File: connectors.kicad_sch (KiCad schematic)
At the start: 1 part, among them J2 SM04B-SRSS-TB

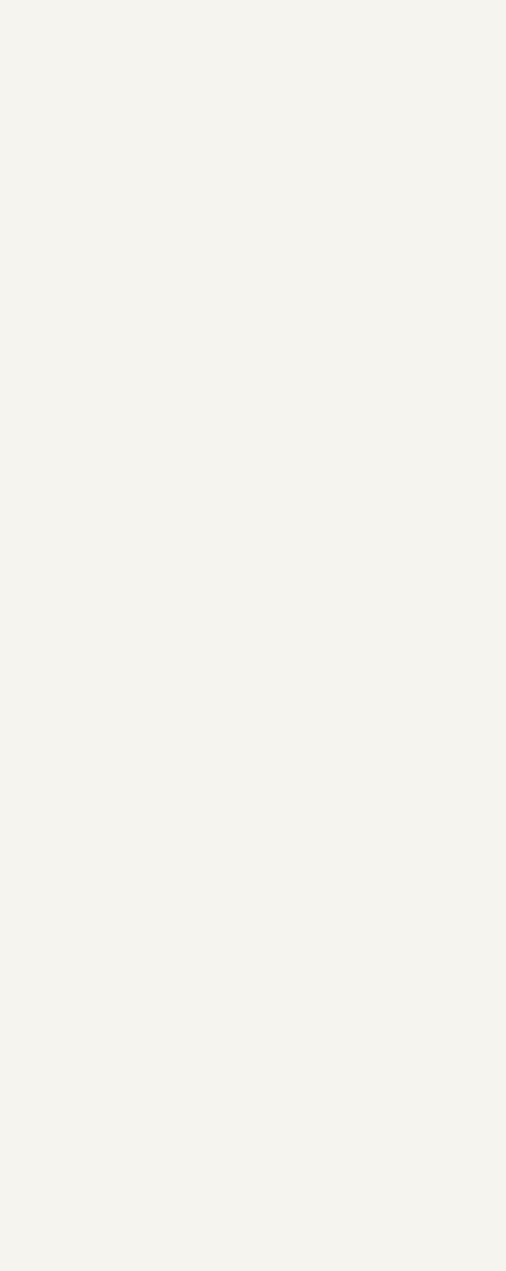
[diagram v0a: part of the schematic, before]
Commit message: finished buck schematic and designed solder pads footprints
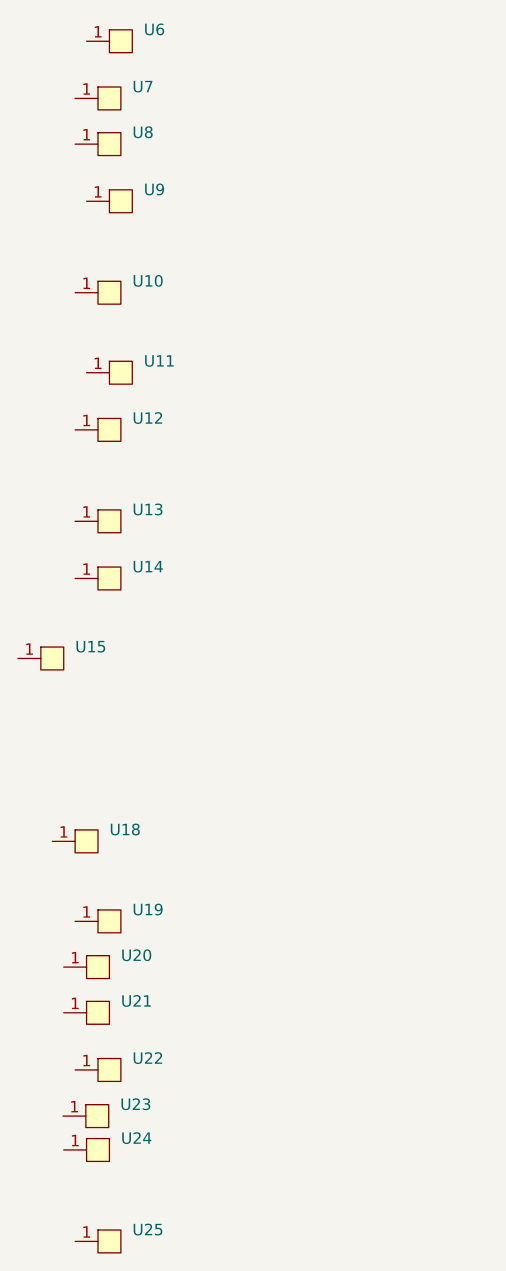
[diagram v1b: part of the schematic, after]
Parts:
- added U10, U11, U12, U13, U14, U15, U18, U19, U20, U21, U22, U23, U24, U25, U6, U7, U8, U9: ~, fcg4_fp:soldering_pad, symbol fcg4:SolderPad

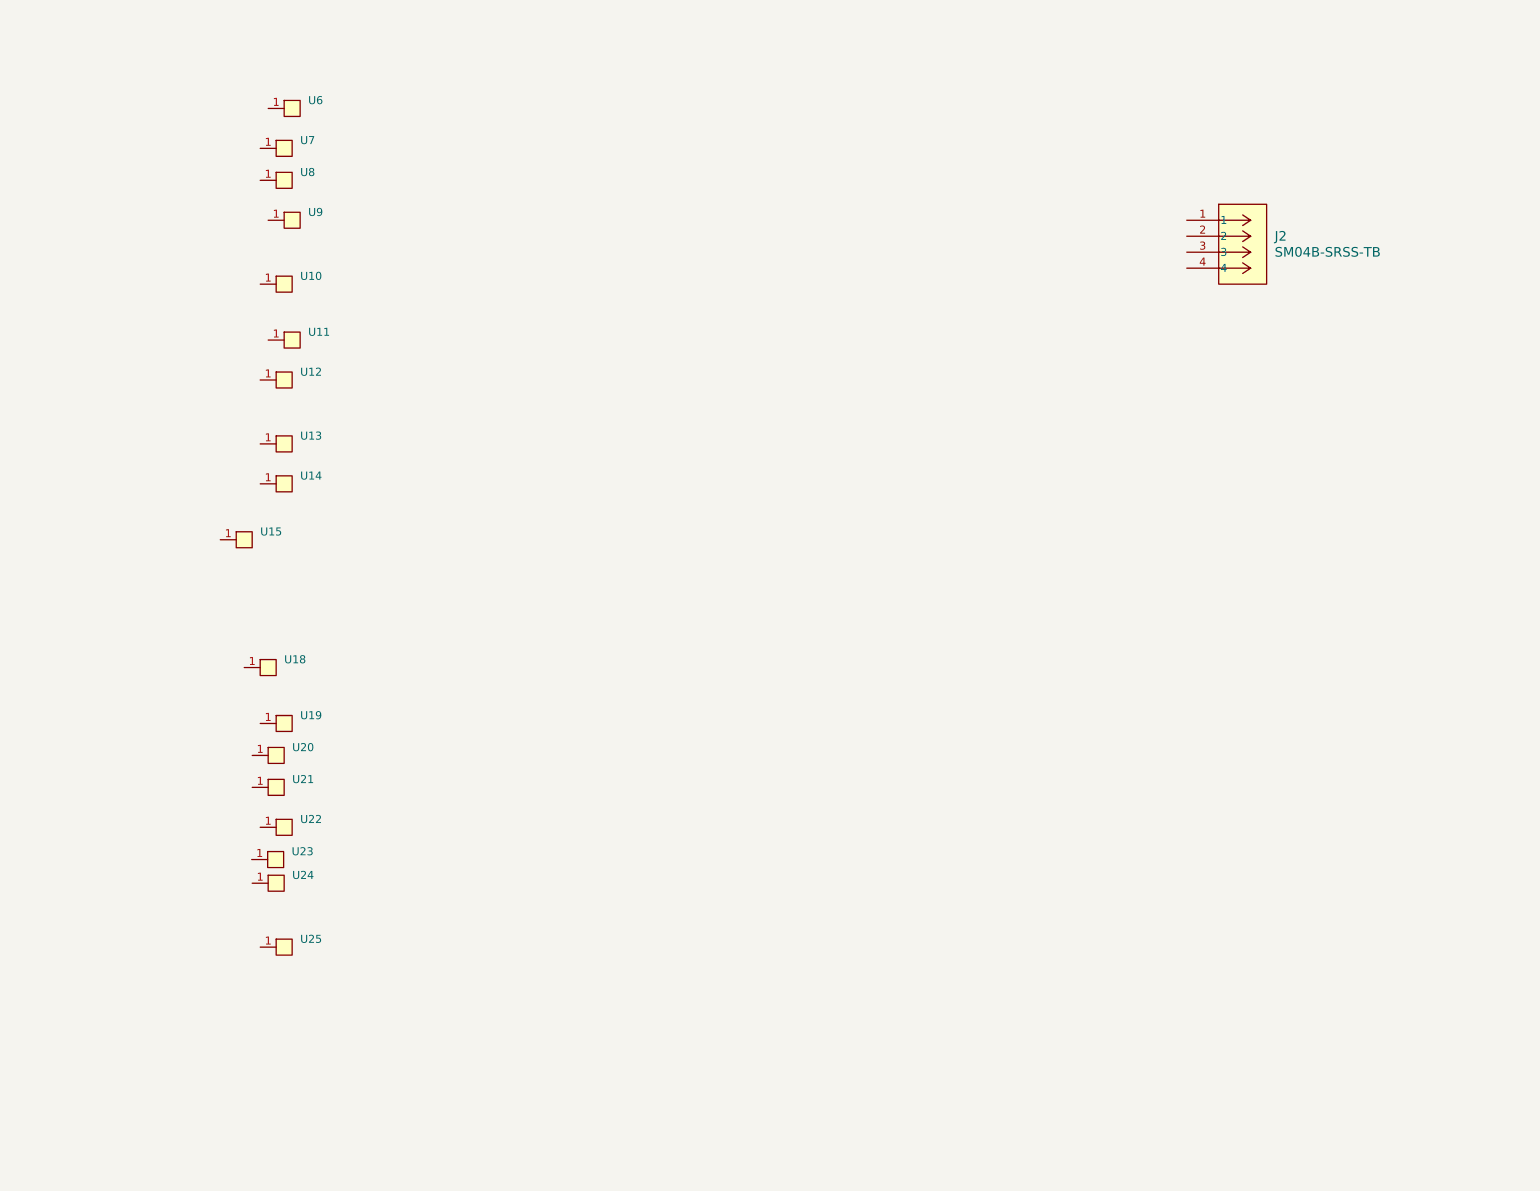
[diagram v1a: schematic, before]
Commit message: add wiring to soldering pads for uart, dji, and esc
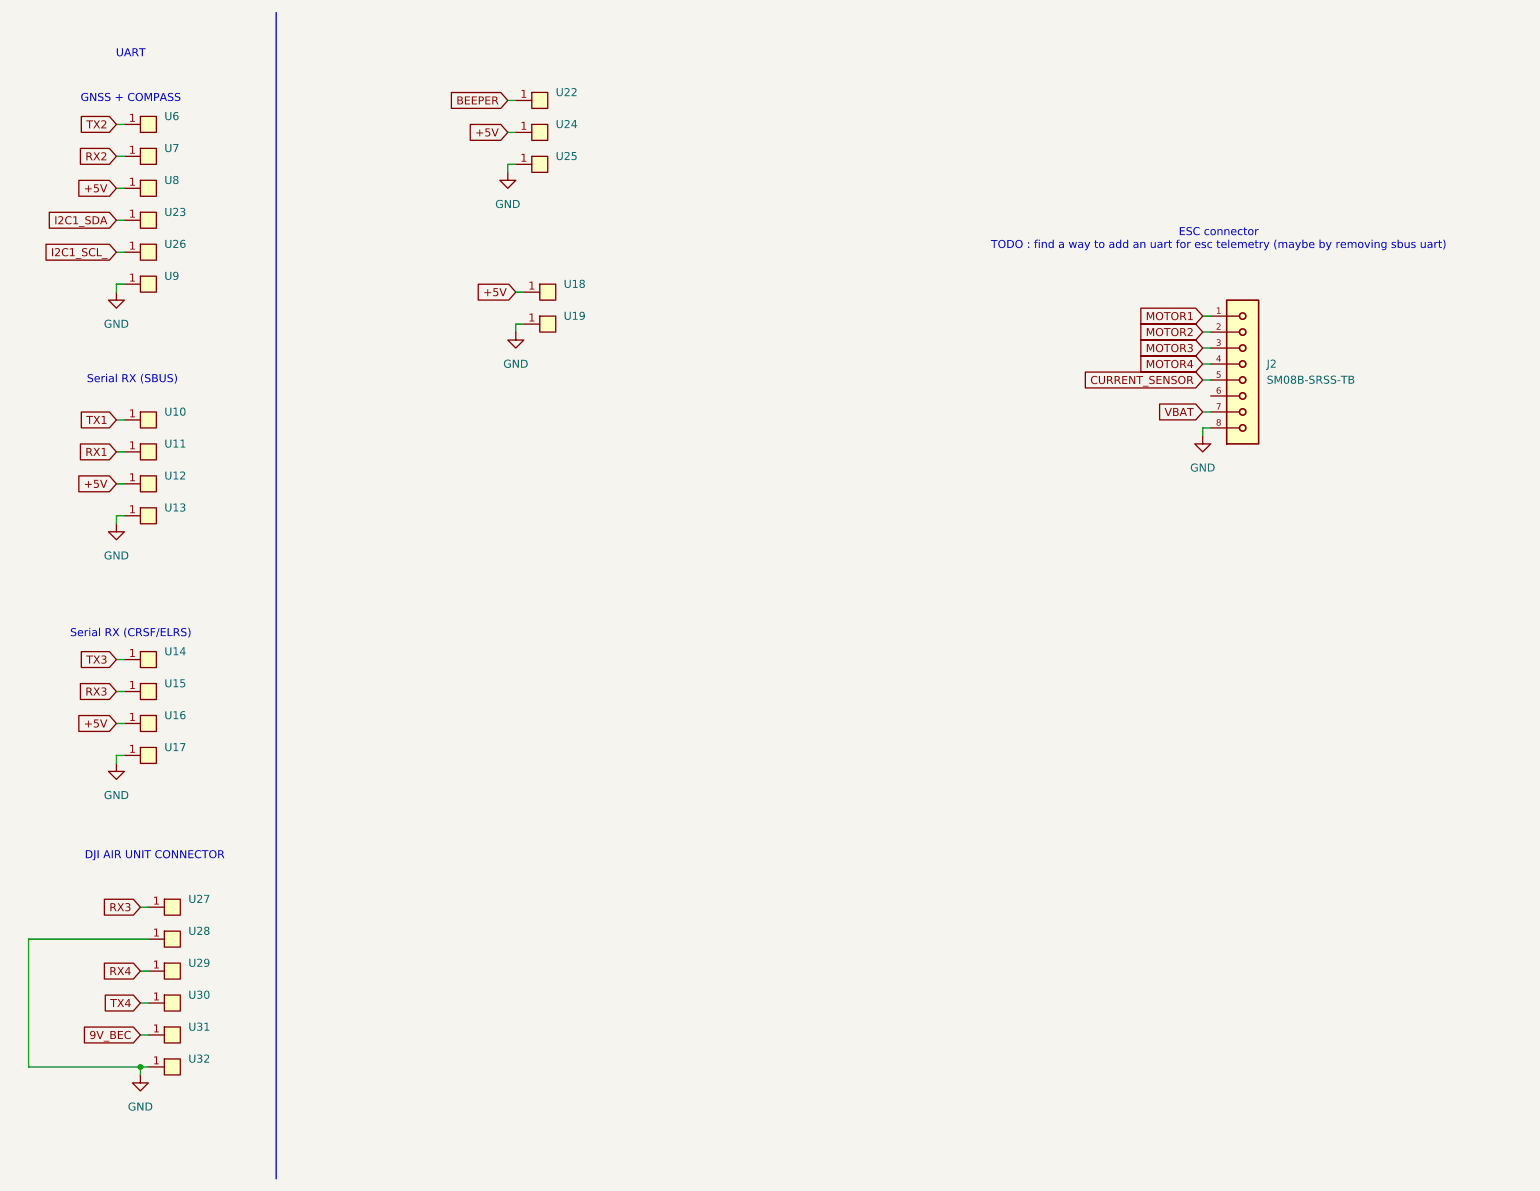
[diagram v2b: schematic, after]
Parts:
- removed J2: SM04B-SRSS-TB, fcg4_fp:CONN_SM04B-SRSS-TB_JST, symbol fcg4:SM04B-SRSS-TB
- removed U20, U21: ~, fcg4_fp:soldering_pad, symbol fcg4:SolderPad
- added J2: SM08B-SRSS-TB, fcg4_fp:JST_SM08B-SRSS-TB, symbol fcg4:SM08B-SRSS-TB
- added U16, U17, U26, U27, U28, U29, U30, U31, U32: ~, fcg4_fp:soldering_pad, symbol fcg4:SolderPad
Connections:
- net RX3: now reaches U15.1
- net RX3: now also U27.1
- net GND: now reaches U13.1
- net GND: now also U19.1, U25.1, U9.1, J2.8, U17.1, U28.1, U32.1
- net BEEPER: now reaches U22.1
- net RX2: now reaches U7.1
- net TX3: now reaches U14.1
- net I2C1_SDA: now reaches U23.1
- net +5V: now reaches U8.1
- net +5V: now also U12.1, U18.1, U24.1, U16.1
- net TX1: now reaches U10.1
- net TX2: now reaches U6.1
- net RX1: now reaches U11.1
- new net 9V_BEC: U31.1
- new net CURRENT_SENSOR: J2.5
- new net I2C1_SCL_: U26.1
- new net MOTOR1: J2.1
- new net MOTOR2: J2.2
- new net MOTOR3: J2.3
- new net MOTOR4: J2.4
- new net RX4: U29.1
- new net TX4: U30.1
- new net VBAT: J2.7
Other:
- note added: "DJI AIR UNIT CONNECTOR"
- note added: "ESC connector TODO : find a way to add an uart for esc telemetry (maybe by removing sbus uart)"
- note added: "GNSS + COMPASS"
- note added: "Serial RX (CRSF/ELRS)"
- note added: "Serial RX (SBUS)"
- note added: "UART"
- moved on the sheet: U6, U7, U8, U9

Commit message: - Removed SBUS receiver support in uart1 and added esc telemetry in uart2 - Added a new Mounting Hole symbol with properties and graphical representation in the schematic (fcg4.kicad_sch). (MountingHoles_30.5x30.5mm_Standard.kicad_mod) with appropriate pads and attributes. - Started PCB editor
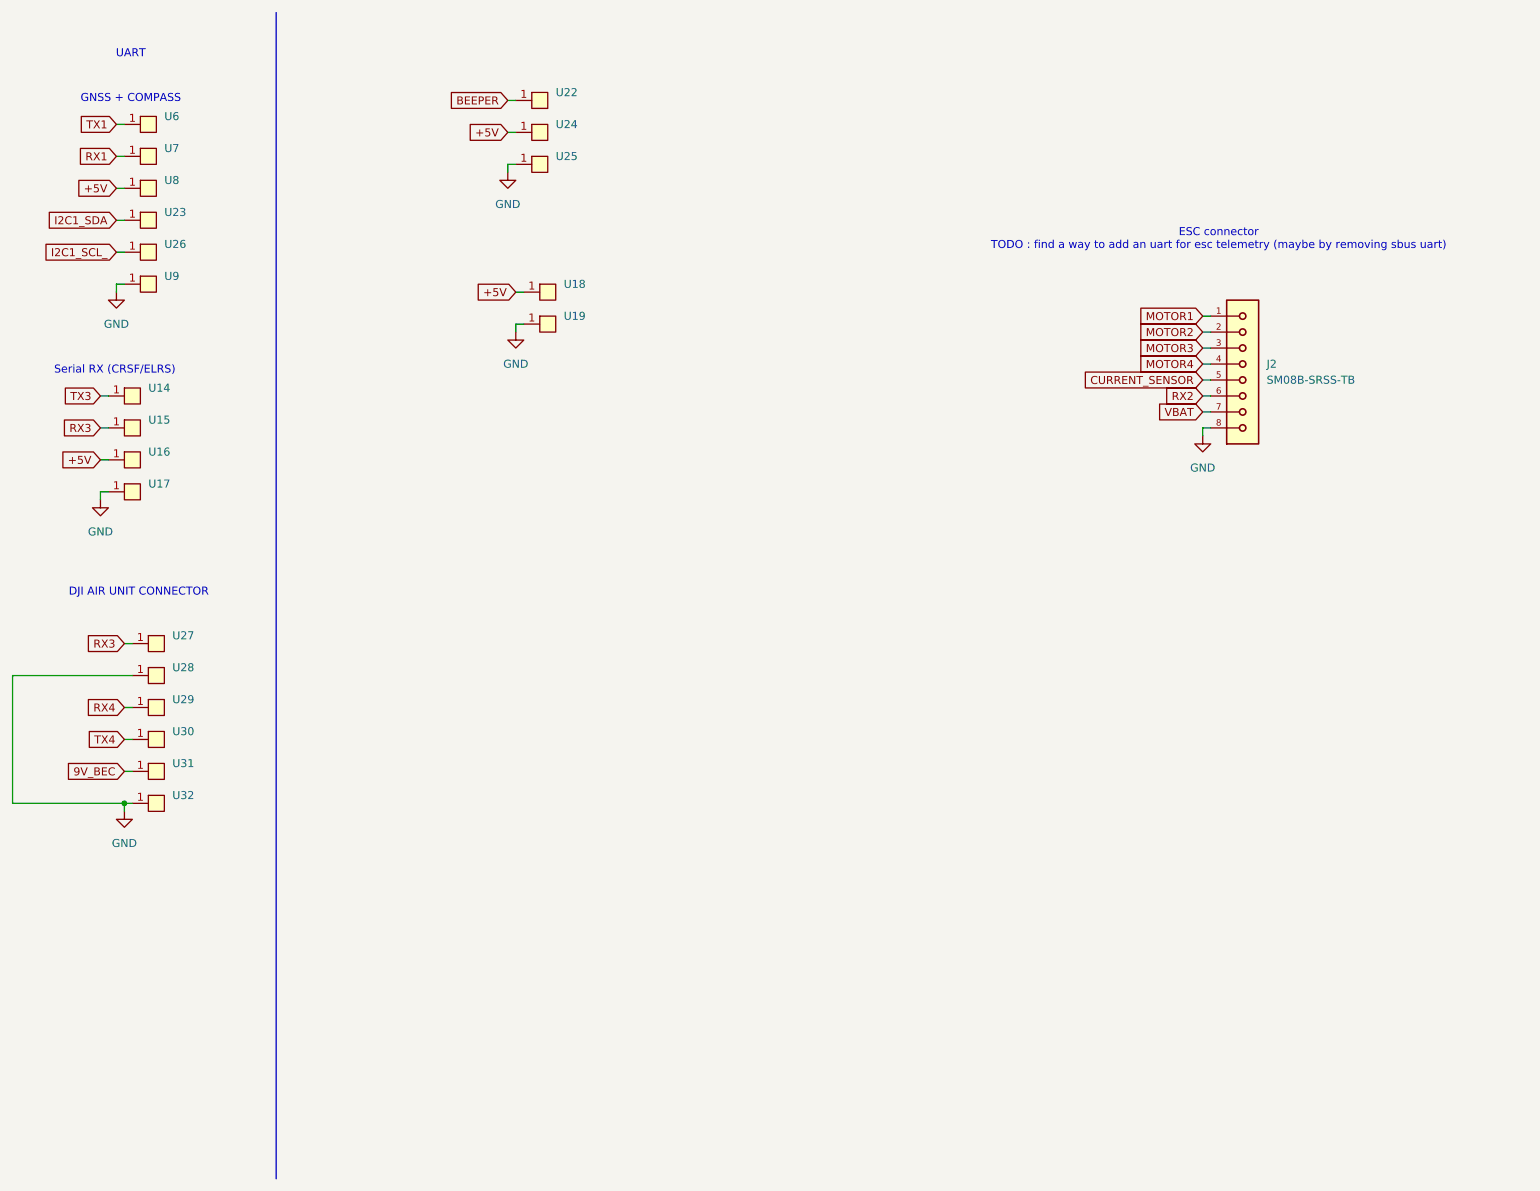
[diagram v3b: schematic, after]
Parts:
- removed U10, U11, U12, U13: ~, fcg4_fp:soldering_pad, symbol fcg4:SolderPad
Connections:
- net TX2 is gone; now on net TX1: U6.1
- net RX1: now also U7.1
- net RX2: now also J2.6; no longer U7.1
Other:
- note removed: "Serial RX (SBUS)"
- moved on the sheet: U14, U15, U16, U17, U27, U28, U29, U30, U31, U32

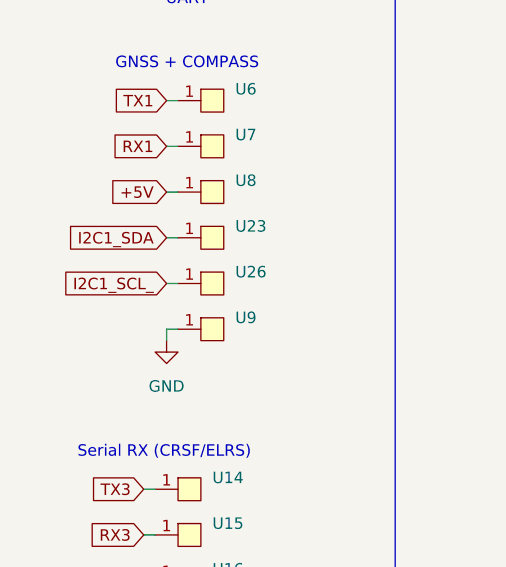
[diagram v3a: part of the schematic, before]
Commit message: - affected footprints for components - started placing components
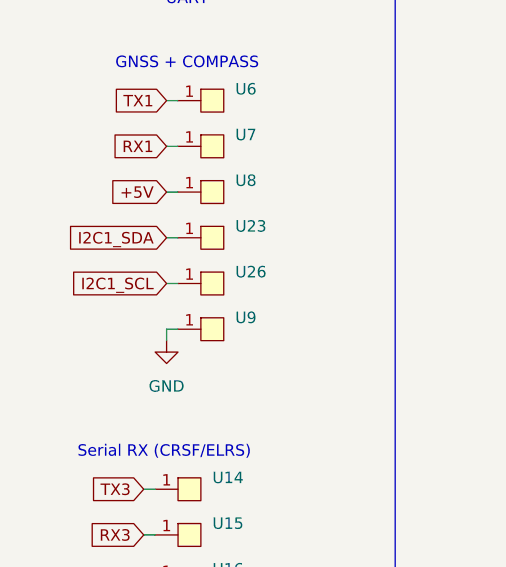
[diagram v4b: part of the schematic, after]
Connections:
- net I2C1_SCL_ renamed I2C1_SCL
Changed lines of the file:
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@@
 		)
 	)
-	(global_label "I2C1_SCL_"
+	(global_label "I2C1_SCL"
 		(shape input)
 		(at 33.02 50.8 180)
@@
 		)
 		(property "Intersheetrefs" "${INTERSHEET_REFS}"
-			(at 20.2982 50.8 0)
+			(at 21.2658 50.8 0)
 			(effects
 				(font

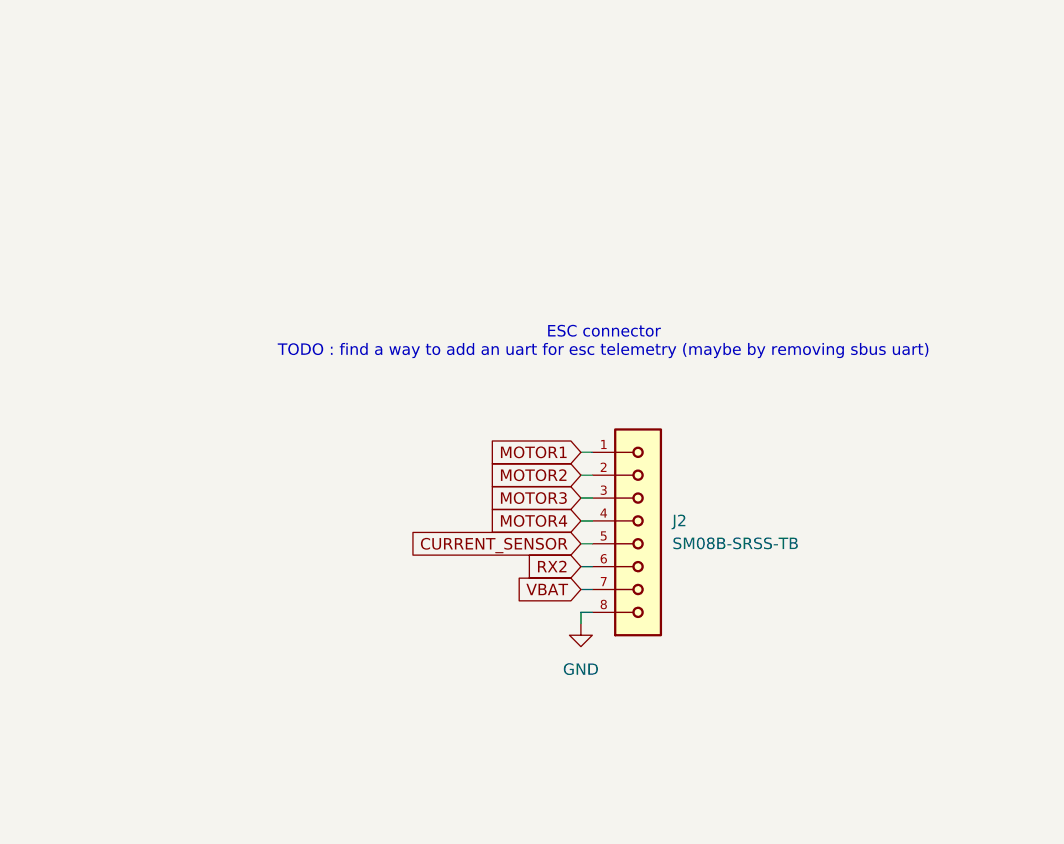
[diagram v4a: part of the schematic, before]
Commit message: add 100ohm for pwm and some routing
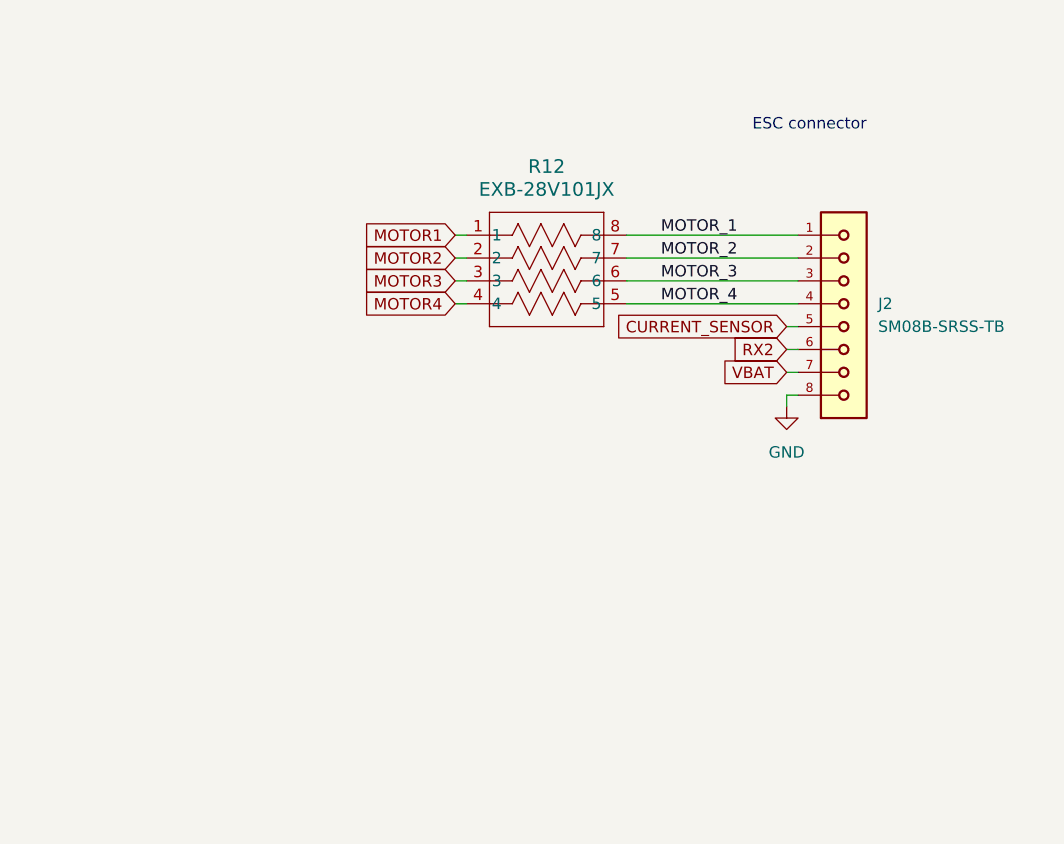
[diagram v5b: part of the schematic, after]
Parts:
- added R12: EXB-28V101JX, fcg4_fp:EXB28V_PAN, symbol fcg4:EXB-28V101JX
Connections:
- net MOTOR1: now also R12.1; no longer J2.1
- net MOTOR2: now also R12.2; no longer J2.2
- net MOTOR3: now also R12.3; no longer J2.3
- net MOTOR4: now also R12.4; no longer J2.4
- new net MOTOR_1: J2.1, R12.8
- new net MOTOR_2: J2.2, R12.7
- new net MOTOR_3: J2.3, R12.6
- new net MOTOR_4: J2.4, R12.5
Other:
- note added: "ESC connector"
- note removed: "ESC connector TODO : find a way to add an uart for esc telemetry (maybe by removing sbus uart)"
- moved on the sheet: J2
